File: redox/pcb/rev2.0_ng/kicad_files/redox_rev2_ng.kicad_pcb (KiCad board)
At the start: 2 copper layers, 162.2 x 138.8 mm, 153 parts, among them J2 OLED-SSD1306, K1 KEYSW, K10 KEYSW, K11 KEYSW, K12 KEYSW, K13 KEYSW, K14 KEYSW, K15 KEYSW, K16 KEYSW, K17 KEYSW, K18 KEYSW, K19 KEYSW, K2 KEYSW, K20 KEYSW, K21 KEYSW, K22 KEYSW, K23 KEYSW, K24 KEYSW, K25 KEYSW, K26 KEYSW, K27 KEYSW, K28 KEYSW, K29 KEYSW, K3 KEYSW, K30 KEYSW, K31 KEYSW, K32 KEYSW, K33 KEYSW, K34 KEYSW, K35 KEYSW, K4 KEYSW, K5 KEYSW, K6 KEYSW, K7 KEYSW, K8 KEYSW, K9 KEYSW, P1 TC2030-AVR, Q1 2N7002, U1 PRTR5V0U2X, U2 ATmega32U4, Y1 16Mhz

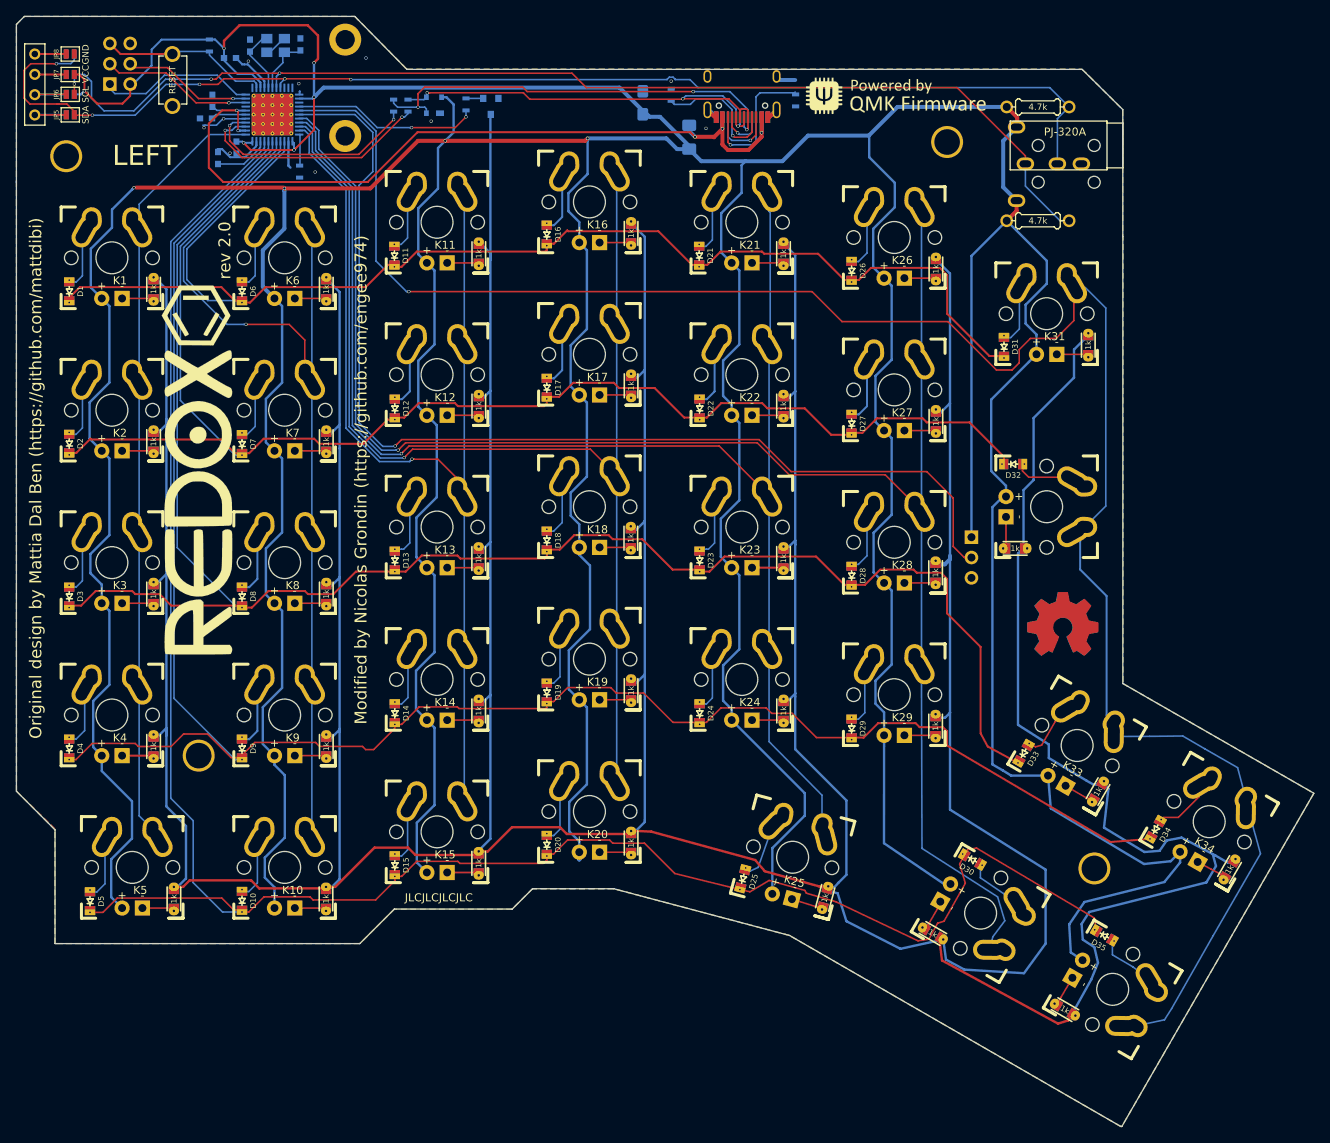
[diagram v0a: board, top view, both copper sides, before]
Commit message: Replace the reset switch footprint by something easier to find - 6x6 push button
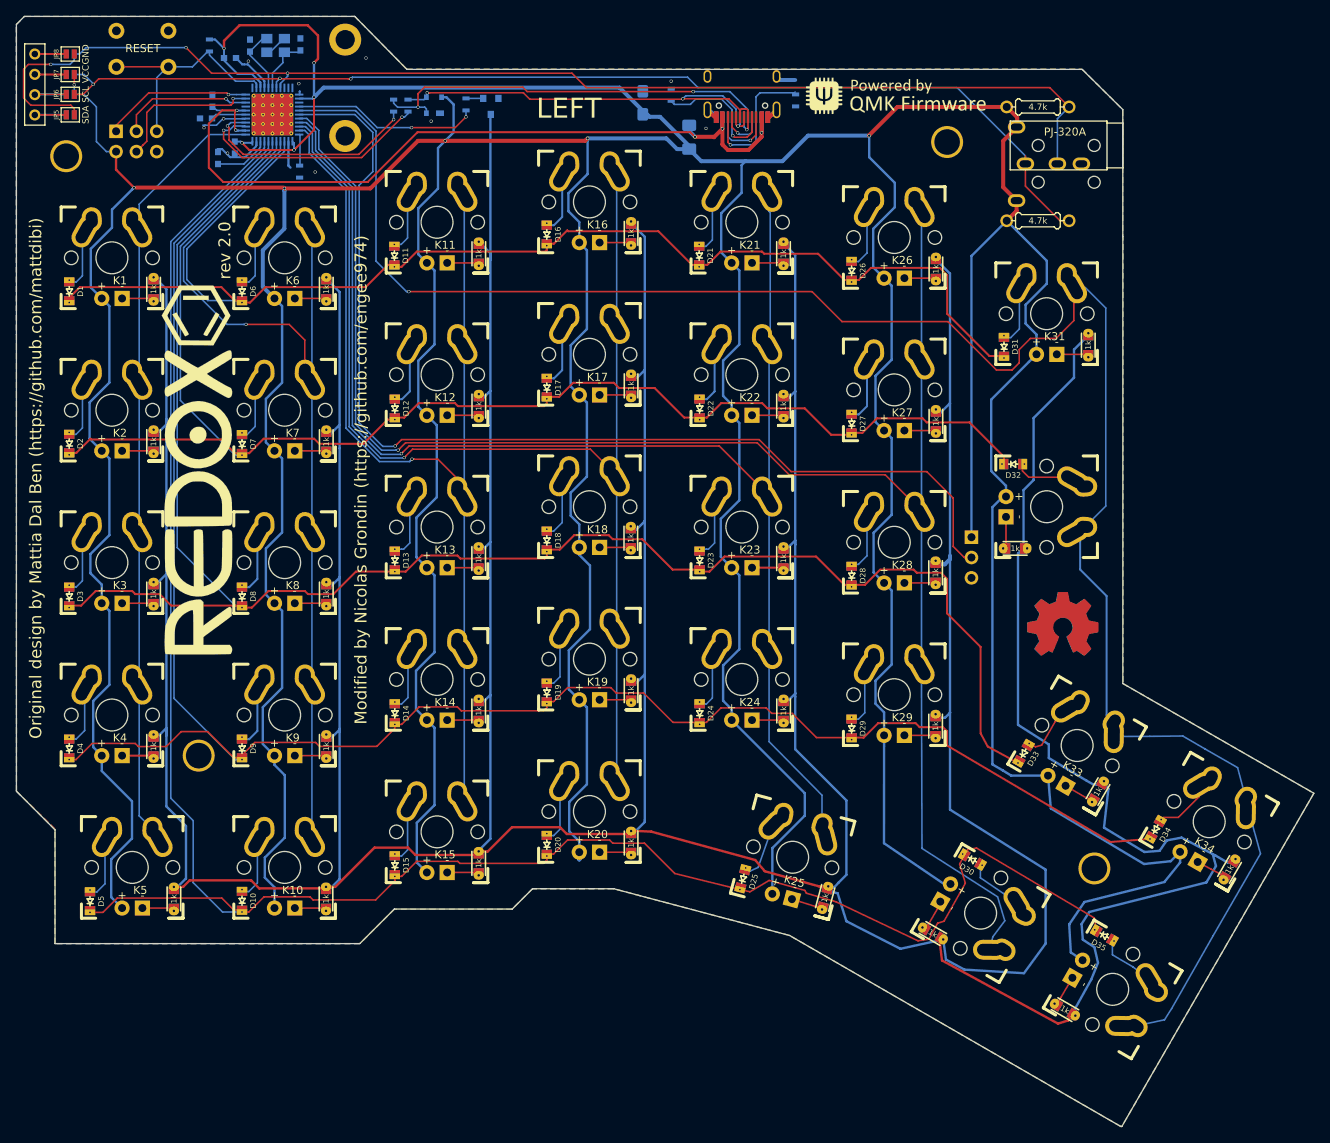
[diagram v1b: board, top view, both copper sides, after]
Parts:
- RST_SW1: footprint redox_footprints:TACT_SWITCH_TVBP06 -> redox_footprints:SW_PUSH_6mm_h4.3mm; moved to B.Cu
- moved RST_SW1 7.19 mm to (92.0, 42.8), turned to 0 degrees
- moved P1 5.95 mm to (92.0, 50.9), turned to 270 degrees
- moved C7 0.20 mm to (106.8, 52.9)
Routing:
- net RST: track 20.9 -> 31.1 mm
- net VCC: track 1051.0 -> 1043.4 mm, vias 10 -> 11
- net SCL: track 143.7 -> 140.1 mm
- net MOSI: track 16.2 -> 18.8 mm
- net SCK: track 19.0 -> 16.7 mm
- net MISO: track 19.7 -> 18.6 mm, vias 0 -> 1
- net SDA: track 155.9 -> 156.5 mm, vias 5 -> 3
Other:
- net class +5V removed
- net class VBUS added: clearance 0.2, trace_width 0.5, via_dia 0.4, via_drill 0.3
- net class VCC: trace_width 0.5 -> 0.3
- board text removed: "JLCJLCJLCJLC"
